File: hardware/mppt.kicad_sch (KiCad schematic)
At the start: 33 parts, among them J1 Conn_01x04_Pin, Q1 BC817, Q2 NTR4171PT1G, U1 INA226

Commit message: updated version
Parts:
- L1: value 2.2m -> 2.2m ( 690mA)
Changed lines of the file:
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@@
 			)
 		)
-		(property "Value" "2.2m"
+		(property "Value" "2.2m ( 690mA)"
 			(at 148.59 64.77 90)
 			(effects

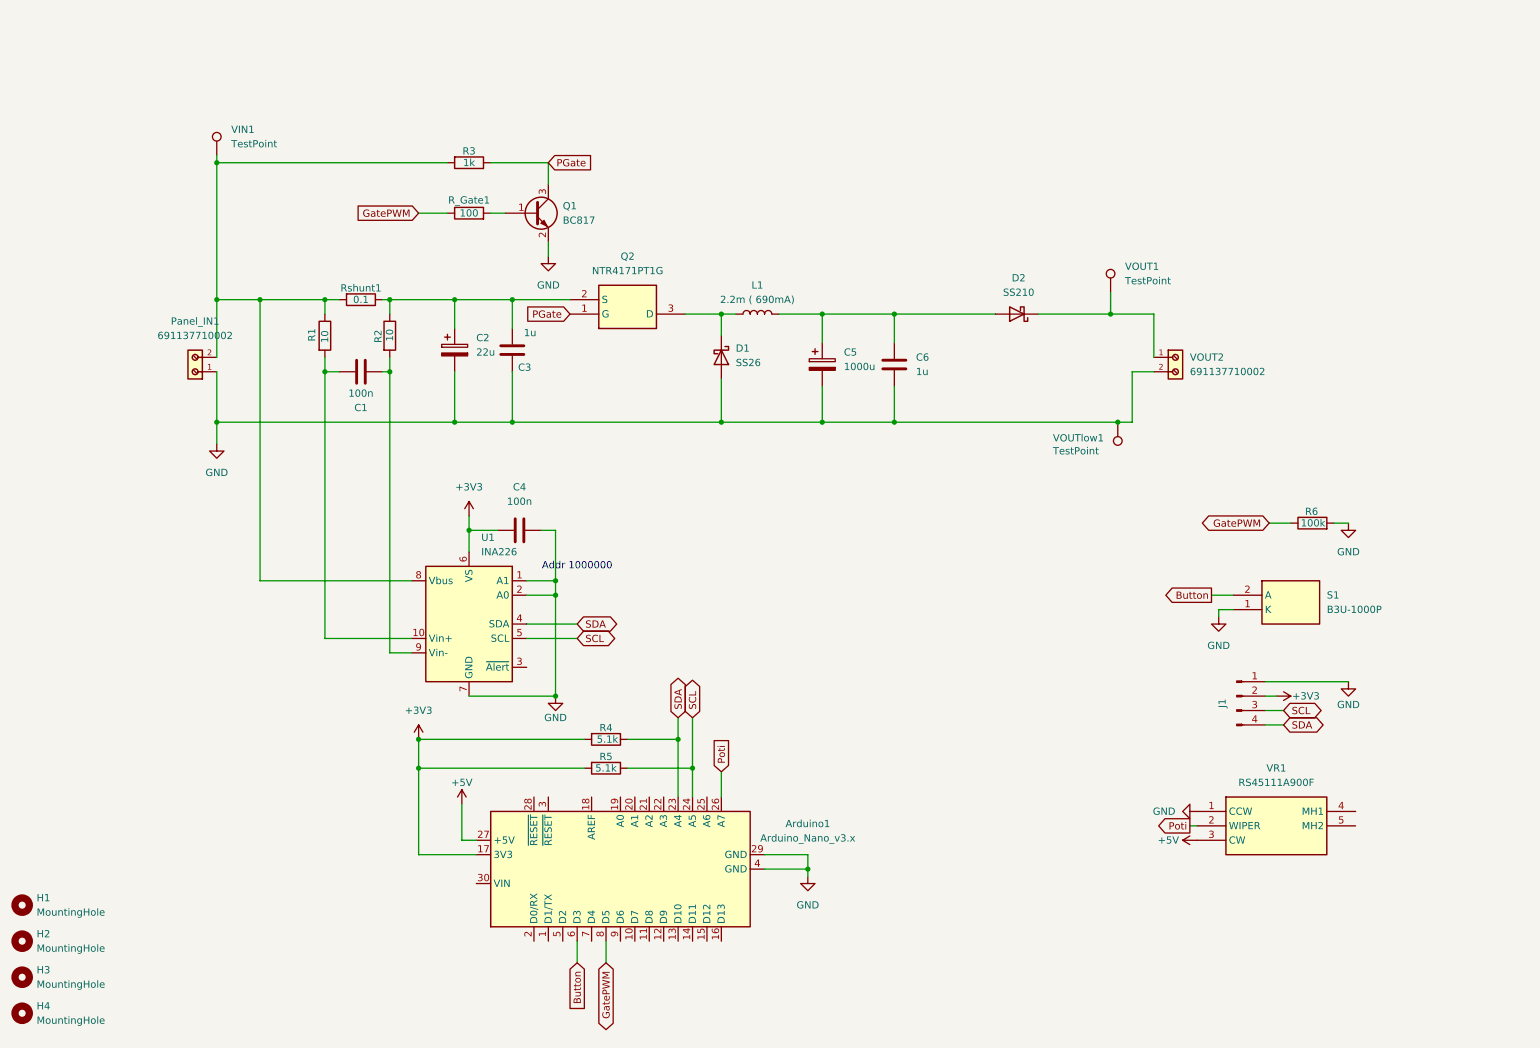
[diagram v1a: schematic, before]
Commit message: added measurment to output
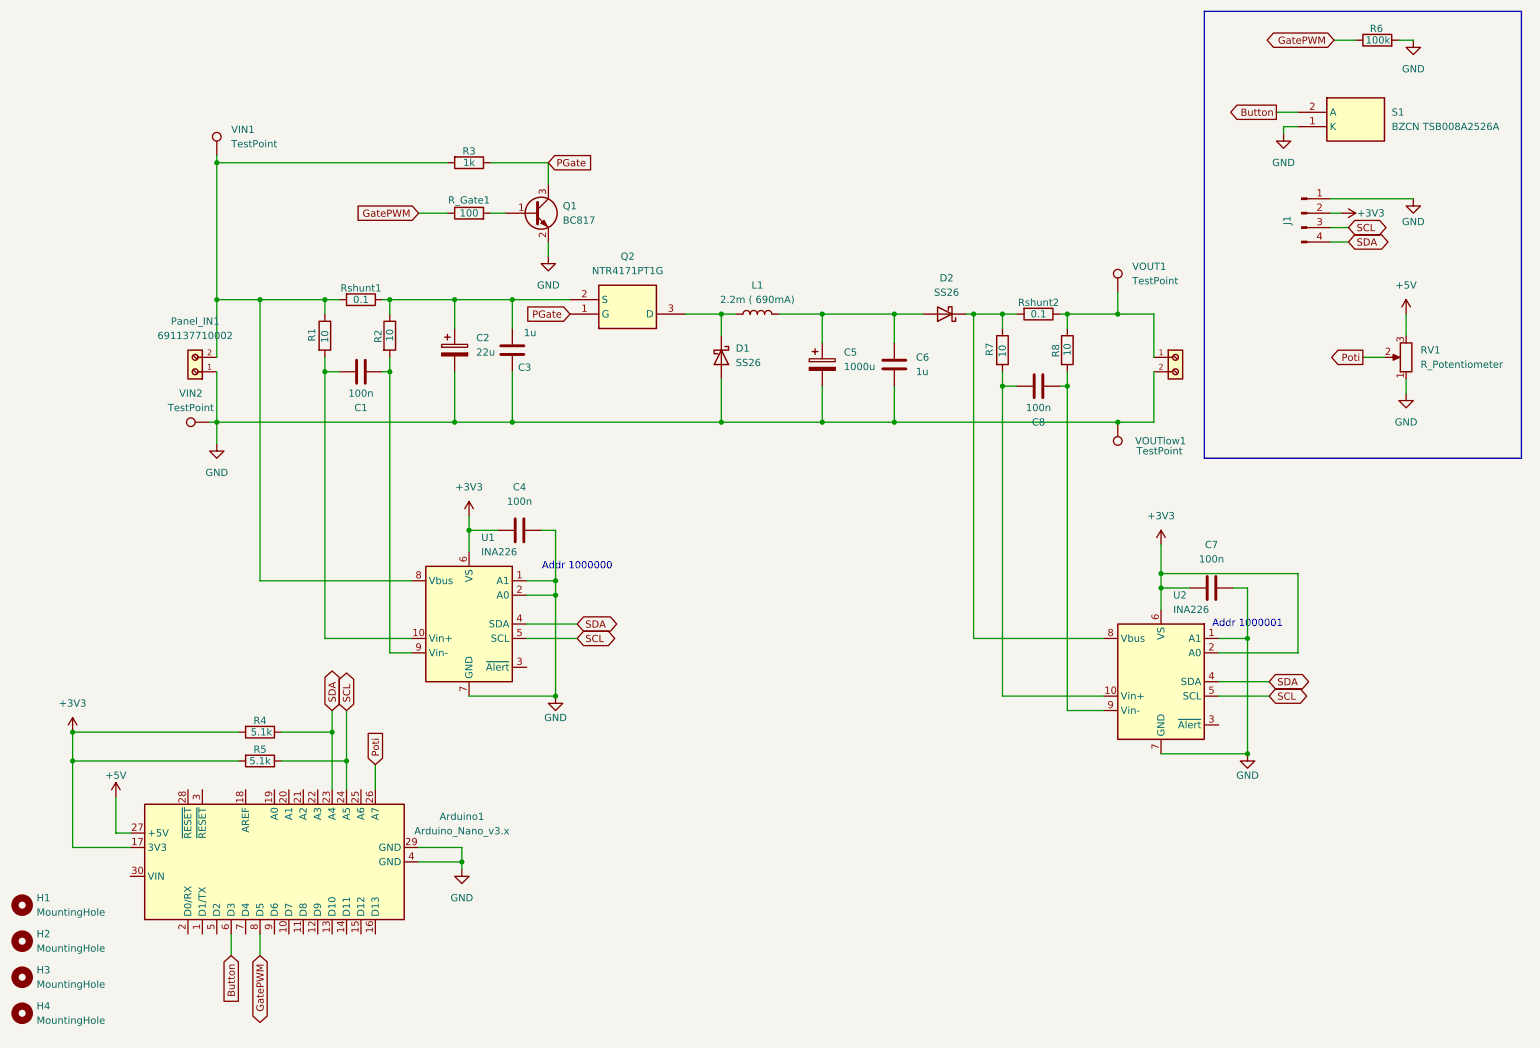
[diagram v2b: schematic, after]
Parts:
- removed D2: SS210, Diode_SMD:D_SMA, symbol Diode:SS210
- removed VR1: RS45111A900F, SamacSys:RS45111A900F, symbol SamacSysParts:RS45111A900F
- added C7, C8: 100n, Capacitor_SMD:C_0805_2012Metric_Pad1.18x1.45mm_HandSolder, symbol Device:C
- added D2: SS26, Diode_SMD:D_SMA, symbol Diode:SS26
- added R7, R8: 10, Resistor_SMD:R_0805_2012Metric_Pad1.20x1.40mm_HandSolder, symbol Device:R
- added RV1: R_Potentiometer, Potentiometer_THT:Potentiometer_Bourns_PTA4543_Single_Slide, symbol Device:R_Potentiometer
- added Rshunt2: 0.1, Resistor_SMD:R_2512_6332Metric_Pad1.40x3.35mm_HandSolder, symbol Device:R
- added U2: INA226, Package_SO:MSOP-10_3x3mm_P0.5mm, symbol Sensor_Energy:INA226
- added VIN2: TestPoint, TestPoint:TestPoint_Keystone_5005-5009_Compact, symbol Connector:TestPoint
- Q2: footprint SOT96P237X111-3N -> Package_TO_SOT_SMD:SOT-23; LCSC Part # (none) -> C28646357
- Rshunt1: LCSC Part # (none) -> C1021528
- S1: value B3U-1000P -> BZCN TSB008A2526A; footprint B3U-1000P -> Button_Switch_SMD:SW_SPST_CK_RS282G05A3; LCSC Part # (none) -> C2888456
- U1: footprint Package_SO:VSSOP-10_3x3mm_P0.5mm -> Package_SO:MSOP-10_3x3mm_P0.5mm; JLCPCB Part # (none) -> C49851
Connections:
- net +3V3: now also C7.1, U2.2 (A0), U2.6 (VS)
- net +5V: now also RV1.3
- net GND: now also C7.2, RV1.1, U2.1 (A1), U2.7 (GND), VIN2.1
- net Poti: now also RV1.2
- net SCL: now also U2.5 (SCL)
- net SDA: now also U2.4 (SDA)
- net at VOUT1.1, VOUT2.1: now also R8.1, Rshunt2.1
- net at C5.1, C6.1, L1.2: now also D2.2 (A)
- new net: C8.1, R7.2, U2.10 (Vin+)
- new net: C8.2, R8.2, U2.9 (Vin-)
- new net: D2.1 (K), R7.1, Rshunt2.2, U2.8 (Vbus)
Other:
- note added: "Addr 1000001"
- moved on the sheet: Arduino1, J1, R4, R5, R6, S1, VOUT1

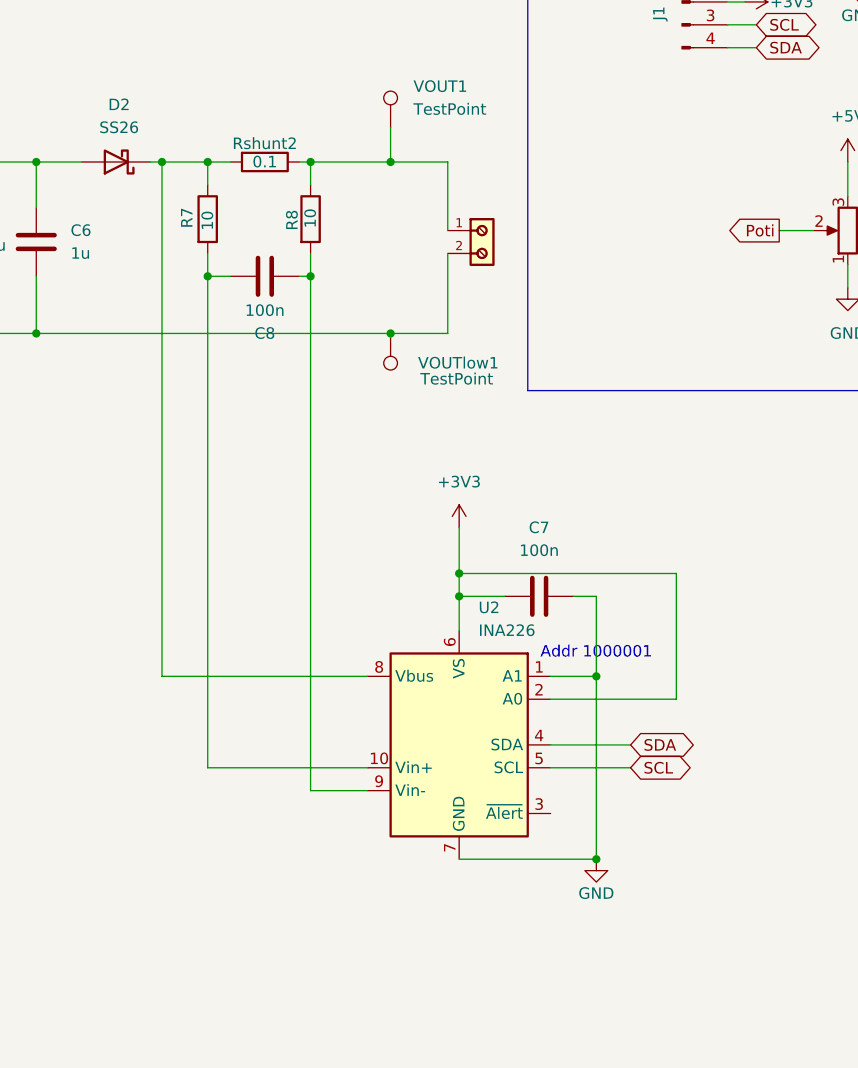
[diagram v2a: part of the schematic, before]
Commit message: added output measurements and adjusted components
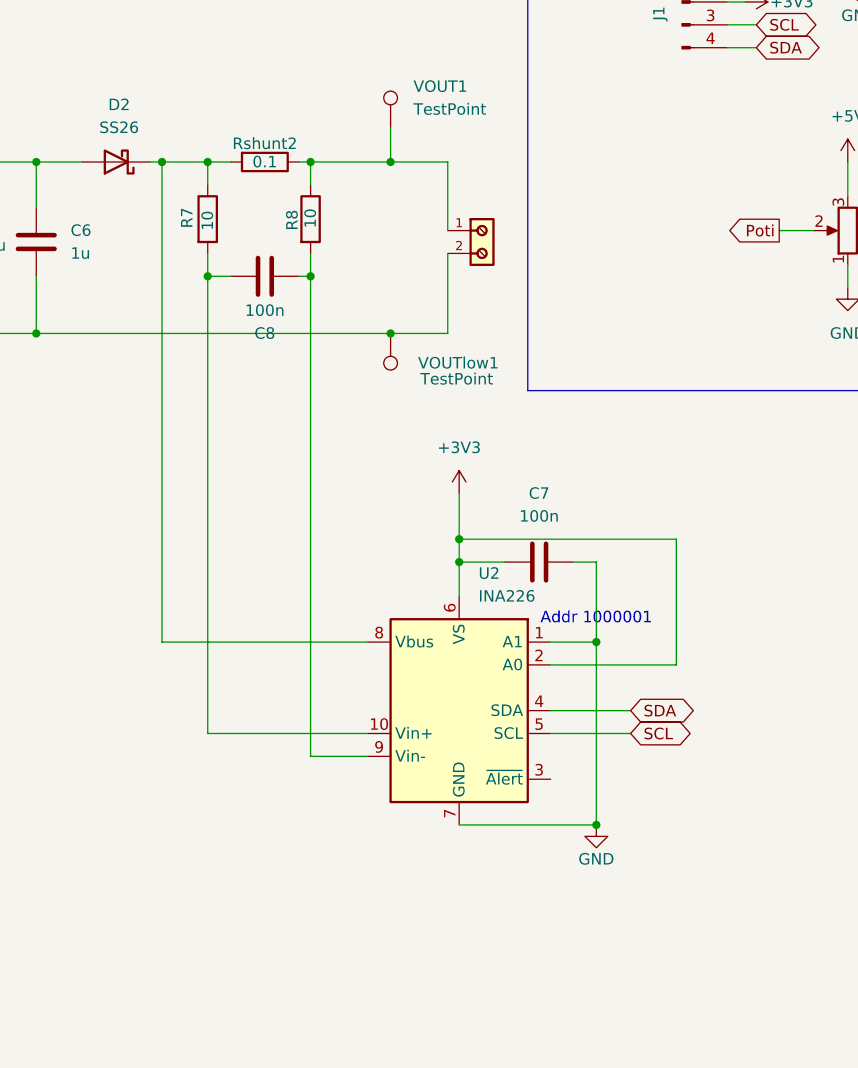
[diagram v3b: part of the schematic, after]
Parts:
- C2: footprint Capacitor_SMD:CP_Elec_6.3x5.9 -> Capacitor_SMD:CP_Elec_6.3x5.4; LCSC Part # C267472 -> C98744
- RV1: JLCPCB Part # (none) -> C17444183
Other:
- moved on the sheet: C7, U2
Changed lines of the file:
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@@
 	(text "Addr 1000001"
 		(exclude_from_sim no)
-		(at 234.95 121.92 0)
+		(at 234.95 118.11 0)
 		(effects
 			(font
@@
 	)
 	(junction
-		(at 234.95 144.78)
+		(at 234.95 140.97)
 		(diameter 0)
 		(color 0 0 0 0)
@@
 	)
 	(junction
-		(at 219.71 113.03)
+		(at 219.71 109.22)
 		(diameter 0)
 		(color 0 0 0 0)
 	)
 	(junction
-		(at 219.71 115.57)
+		(at 219.71 111.76)
 		(diameter 0)
 		(color 0 0 0 0)
@@
 	)
 	(junction
-		(at 234.95 124.46)
+		(at 234.95 120.65)
 		(diameter 0)
 		(color 0 0 0 0)
@@
 	(wire
 		(pts
-			(xy 229.87 132.08) (xy 238.76 132.08)
+			(xy 229.87 128.27) (xy 238.76 128.27)
 		)
 		(stroke
@@
 	(wire
 		(pts
-			(xy 229.87 134.62) (xy 238.76 134.62)
+			(xy 229.87 130.81) (xy 238.76 130.81)
 		)
 		(stroke
@@
 	(wire
 		(pts
-			(xy 229.87 127) (xy 243.84 127)
+			(xy 229.87 123.19) (xy 243.84 123.19)
 		)
 		(stroke
@@
 	(wire
 		(pts
-			(xy 186.69 124.46) (xy 186.69 67.31)
+			(xy 186.69 120.65) (xy 186.69 67.31)
 		)
 		(stroke
@@
 	(wire
 		(pts
-			(xy 229.87 124.46) (xy 234.95 124.46)
+			(xy 229.87 120.65) (xy 234.95 120.65)
 		)
 		(stroke
@@
 	(wire
 		(pts
-			(xy 219.71 115.57) (xy 224.79 115.57)
+			(xy 219.71 111.76) (xy 224.79 111.76)
 		)
 		(stroke
@@
 	(wire
 		(pts
-			(xy 219.71 113.03) (xy 219.71 115.57)
+			(xy 219.71 109.22) (xy 219.71 111.76)
 		)
 		(stroke
@@
 	(wire
 		(pts
-			(xy 191.77 134.62) (xy 191.77 80.01)
+			(xy 191.77 130.81) (xy 191.77 80.01)
 		)
 		(stroke
@@
 	(wire
 		(pts
-			(xy 234.95 124.46) (xy 234.95 144.78)
+			(xy 234.95 120.65) (xy 234.95 140.97)
 		)
 		(stroke
@@
 	(wire
 		(pts
-			(xy 219.71 115.57) (xy 219.71 119.38)
+			(xy 219.71 111.76) (xy 219.71 115.57)
 		)
 		(stroke
@@
 	(wire
 		(pts
-			(xy 243.84 113.03) (xy 219.71 113.03)
+			(xy 243.84 109.22) (xy 219.71 109.22)
 		)
 		(stroke
@@
 	(wire
 		(pts
-			(xy 234.95 115.57) (xy 232.41 115.57)
+			(xy 234.95 111.76) (xy 232.41 111.76)
 		)
 		(stroke
@@
 	(wire
 		(pts
-			(xy 203.2 137.16) (xy 203.2 80.01)
+			(xy 203.2 133.35) (xy 203.2 80.01)
 		)
 		(stroke
@@
 	(wire
 		(pts
-			(xy 243.84 127) (xy 243.84 113.03)
+			(xy 243.84 123.19) (xy 243.84 109.22)
 		)
 		(stroke
@@
 	(wire
 		(pts
-			(xy 209.55 134.62) (xy 191.77 134.62)
+			(xy 209.55 130.81) (xy 191.77 130.81)
 		)
 		(stroke
@@
 	(wire
 		(pts
-			(xy 234.95 115.57) (xy 234.95 124.46)
+			(xy 234.95 111.76) (xy 234.95 120.65)
 		)
 		(stroke
@@
 	(wire
 		(pts
-			(xy 219.71 144.78) (xy 234.95 144.78)
+			(xy 219.71 140.97) (xy 234.95 140.97)
 		)
 		(stroke
@@
 	(wire
 		(pts
-			(xy 219.71 107.95) (xy 219.71 113.03)
+			(xy 219.71 104.14) (xy 219.71 109.22)
 		)
 		(stroke
@@
 	(wire
 		(pts
-			(xy 209.55 124.46) (xy 186.69 124.46)
+			(xy 209.55 120.65) (xy 186.69 120.65)
 		)
 		(stroke
@@
 	(wire
 		(pts
-			(xy 209.55 137.16) (xy 203.2 137.16)
+			(xy 209.55 133.35) (xy 203.2 133.35)
 		)
 		(stroke
@@
 	(global_label "SDA"
 		(shape bidirectional)
-		(at 238.76 132.08 0)
+		(at 238.76 128.27 0)
 		(fields_autoplaced yes)
 		(effects
@@
 		)
 		(property "Intersheetrefs" "${INTERSHEET_REFS}"
-			(at 246.4246 132.08 0)
+			(at 246.4246 128.27 0)
 			(effects
 				(font
@@
 	(global_label "SCL"
 		(shape bidirectional)
-		(at 238.76 134.62 0)
+		(at 238.76 130.81 0)
 		(fields_autoplaced yes)
 		(effects
@@
 		)
 		(property "Intersheetrefs" "${INTERSHEET_REFS}"
-			(at 246.3641 134.62 0)
+			(at 246.3641 130.81 0)
 			(effects
 				(font
@@
 	(symbol
 		(lib_id "power:GND")
-		(at 234.95 144.78 0)
+		(at 234.95 140.97 0)
 		(unit 1)
 		(exclude_from_sim no)
@@
 		(dnp no)
 		(property "Reference" "#PWR09"
-			(at 234.95 151.13 0)
+			(at 234.95 147.32 0)
 			(effects
 				(font
@@
 		)
 		(property "Value" "GND"
-			(at 234.95 148.59 0)
+			(at 234.95 144.78 0)
 			(effects
 				(font
@@
 		)
 		(property "Footprint" ""
-			(at 234.95 144.78 0)
+			(at 234.95 140.97 0)
 			(effects
 				(font
@@
 		)
 		(property "Datasheet" ""
-			(at 234.95 144.78 0)
+			(at 234.95 140.97 0)
 			(effects
 				(font
@@
 		)
 		(property "Description" "Power symbol creates a global label with name \"GND\" , ground"
-			(at 234.95 144.78 0)
+			(at 234.95 140.97 0)
 			(effects
 				(font
@@
 	(symbol
 		(lib_id "power:+3V3")
-		(at 219.71 107.95 0)
+		(at 219.71 104.14 0)
 		(unit 1)
 		(exclude_from_sim no)
@@
 		(fields_autoplaced yes)
 		(property "Reference" "#PWR08"
-			(at 219.71 111.76 0)
+			(at 219.71 107.95 0)
 			(effects
 				(font
@@
 		)
 		(property "Value" "+3V3"
-			(at 219.71 102.87 0)
+			(at 219.71 99.06 0)
 			(effects
 				(font
@@
 		)
 		(property "Footprint" ""
-			(at 219.71 107.95 0)
+			(at 219.71 104.14 0)
 			(effects
 				(font
@@
 		)
 		(property "Datasheet" ""
-			(at 219.71 107.95 0)
+			(at 219.71 104.14 0)
 			(effects
 				(font
@@
 		)
 		(property "Description" "Power symbol creates a global label with name \"+3V3\""
-			(at 219.71 107.95 0)
+			(at 219.71 104.14 0)
 			(effects
 				(font
@@
 			)
 		)
-		(property "Footprint" "Capacitor_SMD:CP_Elec_6.3x5.9"
+		(property "Footprint" "Capacitor_SMD:CP_Elec_6.3x5.4"
 			(at 96.2152 77.47 0)
 			(effects
@@
 			)
 		)
-		(property "LCSC Part #" "C267472"
+		(property "LCSC Part #" "C98744"
 			(at 95.25 73.66 0)
 			(effects
@@
 			)
 		)
+		(property "JLCPCB Part #" "C17444183"
+			(at 262.89 74.93 0)
+			(effects
+				(font
+					(size 1.27 1.27)
+				)
+				(hide yes)
+			)
+		)
 		(pin "3"
 		)
@@
 	(symbol
 		(lib_id "Device:C")
-		(at 228.6 115.57 90)
+		(at 228.6 111.76 90)
 		(unit 1)
 		(exclude_from_sim no)
@@
 		(fields_autoplaced yes)
 		(property "Reference" "C7"
-			(at 228.6 107.95 90)
+			(at 228.6 104.14 90)
 			(effects
 				(font
@@
 		)
 		(property "Value" "100n"
-			(at 228.6 110.49 90)
+			(at 228.6 106.68 90)
 			(effects
 				(font
@@
 		)
 		(property "Footprint" "Capacitor_SMD:C_0805_2012Metric_Pad1.18x1.45mm_HandSolder"
-			(at 232.41 114.6048 0)
+			(at 232.41 110.7948 0)
 			(effects
 				(font
@@
 		)
 		(property "Datasheet" "~"
-			(at 228.6 115.57 0)
+			(at 228.6 111.76 0)
 			(effects
 				(font
@@
 		)
 		(property "Description" "Unpolarized capacitor"
-			(at 228.6 115.57 0)
+			(at 228.6 111.76 0)
 			(effects
 				(font
@@
 		)
 		(property "LCSC Part #" "C49678"
-			(at 228.6 115.57 90)
+			(at 228.6 111.76 90)
 			(effects
 				(font
@@
 	(symbol
 		(lib_id "Sensor_Energy:INA226")
-		(at 219.71 132.08 0)
+		(at 219.71 128.27 0)
 		(unit 1)
 		(exclude_from_sim no)
@@
 		(fields_autoplaced yes)
 		(property "Reference" "U2"
-			(at 221.8533 116.84 0)
+			(at 221.8533 113.03 0)
 			(effects
 				(font
@@
 		)
 		(property "Value" "INA226"
-			(at 221.8533 119.38 0)
+			(at 221.8533 115.57 0)
 			(effects
 				(font
@@
 		)
 		(property "Footprint" "Package_SO:MSOP-10_3x3mm_P0.5mm"
-			(at 240.03 143.51 0)
+			(at 240.03 139.7 0)
 			(effects
 				(font
@@
 		)
 		(property "Datasheet" "http://www.ti.com/lit/ds/symlink/ina226.pdf"
-			(at 228.6 134.62 0)
+			(at 228.6 130.81 0)
 			(effects
 				(font
@@
 		)
 		(property "Description" "High-Side or Low-Side Measurement, Bi-Directional Current and Power Monitor (0-36V) with I2C Compatible Interface, VSSOP-10"
-			(at 219.71 132.08 0)
+			(at 219.71 128.27 0)
 			(effects
 				(font
@@
 		)
 		(property "JLCPCB Part #" "C49851"
-			(at 219.71 132.08 0)
+			(at 219.71 128.27 0)
 			(effects
 				(font
